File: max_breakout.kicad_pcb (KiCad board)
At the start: 4 copper layers, 51.1 x 25.7 mm, 47 parts, among them J1 USB_B_Micro, J2 Left, J3 AVR-JTAG-10, J4 Right, SW1 User, SW2 Reset, U1 LP2985-5.0, U2 LP2985-3.3, U4 MAX40203AUK+T, U5 74HCT125, U7 EPM7032STC44, U8 74HCT1G04, X1 CTX-636 50mhz

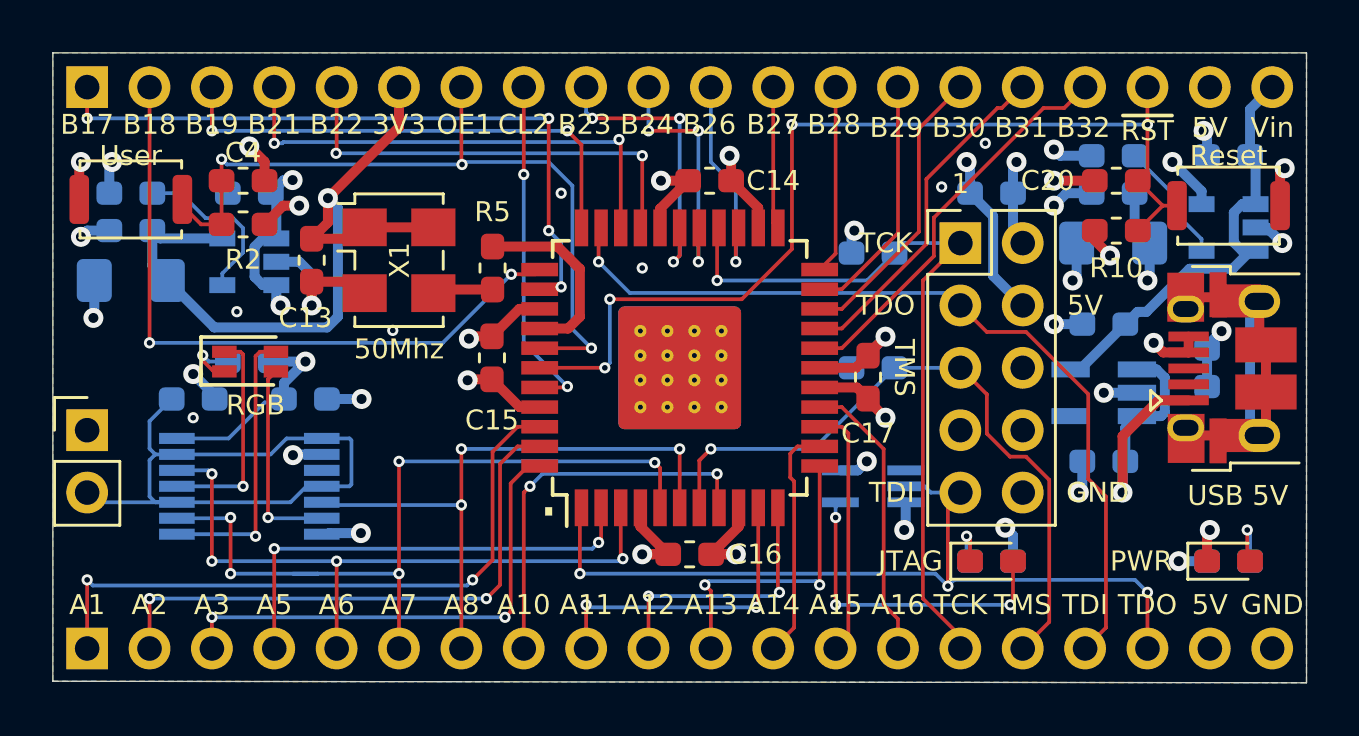
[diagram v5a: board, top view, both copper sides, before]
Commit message: removed extra cap from reg outputs
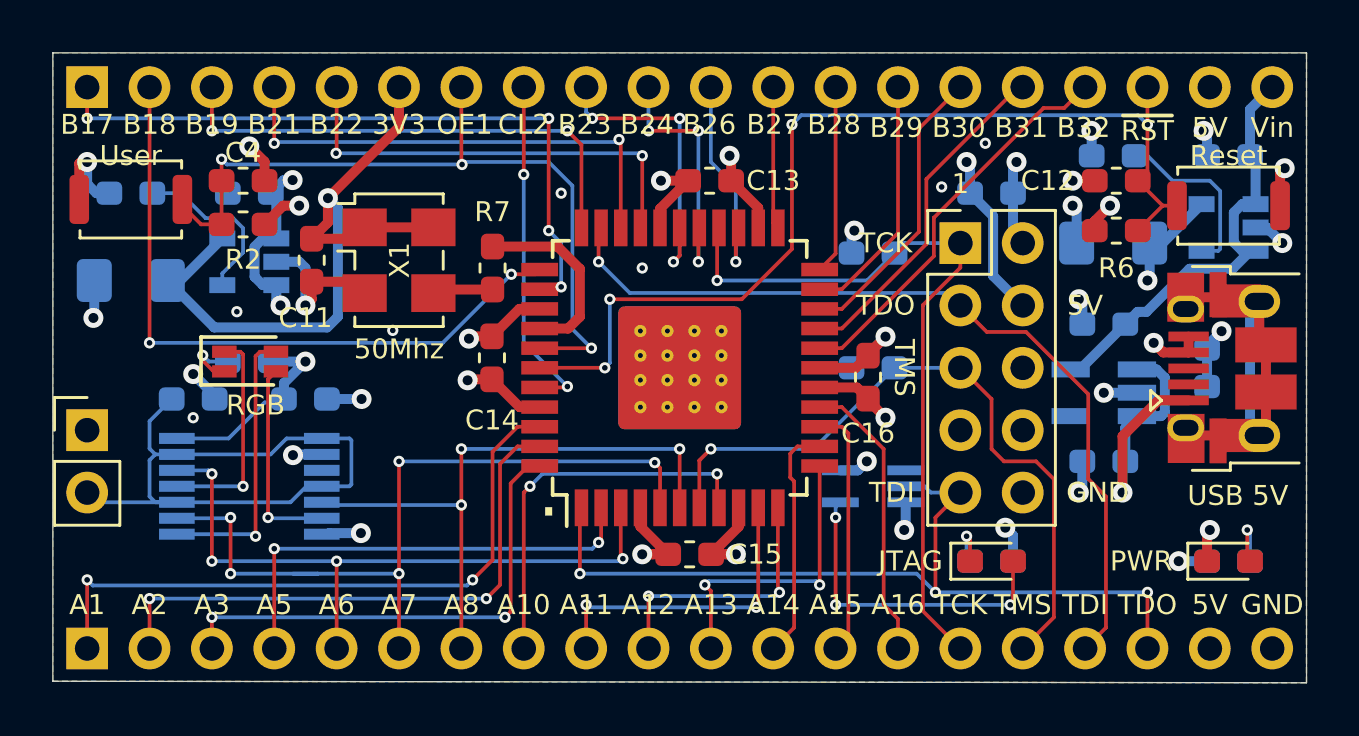
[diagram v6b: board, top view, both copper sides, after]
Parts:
- removed the C8 at (167.5, 97.0)
- removed the C9 at (127.5, 98.6)
- renumbered C12 to C10, C13 to C11, C20 to C12, C14 to C13, C15 to C14, C16 to C15, C17 to C16, C18 to C17, C19 to C18, C10 to C8, C11 to C9, R8 to R10, R9 to R3, R3 to R4, R4 to R5, R10 to R6, R5 to R7, R6 to R8, R7 to R9, U4 to U3, U5 to U4, U7 to U5, U8 to U6
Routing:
- net GND: track 58.9 -> 55.6 mm, vias 37 -> 34
- net 3V3: track 31.0 -> 28.7 mm
- net Net-(C6-Pad1): track 5.00 -> 7.23 mm
- net 5V: track 50.6 -> 49.0 mm, vias 15 -> 14
- net /TMS: track 27.9 -> 28.4 mm

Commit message: Replaced RGB with leds. Reorganized switches. pulldowns for OE and RST
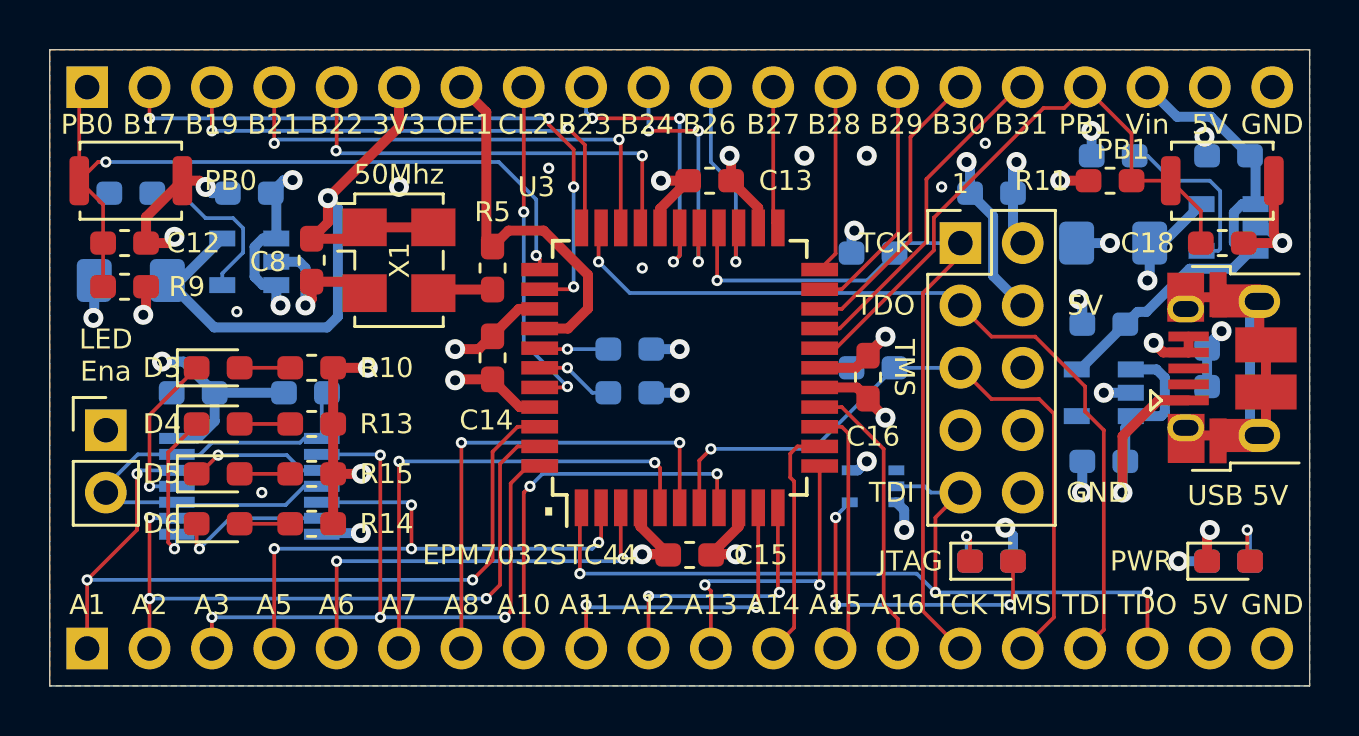
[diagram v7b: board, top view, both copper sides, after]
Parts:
- removed the C11 at (134.9, 99.8)
- removed the C4 at (132.1, 96.5)
- removed the J3 at (161.3, 99.1)
- removed the R2 at (132.1, 98.3)
- removed the U5 at (149.9, 104.1)
- added C18: 10nF, Capacitor_SMD:C_0603_1608Metric_Pad1.05x0.95mm_HandSolder, F.Cu at (172.0, 99.1)
- added C8: 100nF, Capacitor_SMD:C_0603_1608Metric_Pad1.05x0.95mm_HandSolder, F.Cu at (134.9, 99.8)
- added D4: Grn, LED_SMD:LED_0603_1608Metric_Pad1.05x0.95mm_HandSolder, F.Cu at (131.1, 106.4)
- added D5: Grn, LED_SMD:LED_0603_1608Metric_Pad1.05x0.95mm_HandSolder, F.Cu at (131.1, 108.5)
- added D6: Grn, LED_SMD:LED_0603_1608Metric_Pad1.05x0.95mm_HandSolder, F.Cu at (131.1, 110.5)
- added J2: AVR-JTAG-10, Connector_PinHeader_2.54mm:PinHeader_2x05_P2.54mm_Vertical, F.Cu at (161.3, 99.1)
- added R10: 360R, Resistor_SMD:R_0603_1608Metric_Pad1.05x0.95mm_HandSolder, F.Cu at (134.9, 104.1)
- added R11: 10K, Resistor_SMD:R_0603_1608Metric_Pad1.05x0.95mm_HandSolder, F.Cu at (167.4, 96.5)
- added R13: 360R, Resistor_SMD:R_0603_1608Metric_Pad1.05x0.95mm_HandSolder, F.Cu at (134.9, 106.4)
- added R14: 360R, Resistor_SMD:R_0603_1608Metric_Pad1.05x0.95mm_HandSolder, F.Cu at (134.9, 110.5)
- added R15: 360R, Resistor_SMD:R_0603_1608Metric_Pad1.05x0.95mm_HandSolder, F.Cu at (134.9, 108.5)
- added R9: 10K, Resistor_SMD:R_0603_1608Metric_Pad1.05x0.95mm_HandSolder, F.Cu at (127.3, 100.8)
- added U3: EPM7032STC44, Package_QFP:TQFP-44_10x10mm_P0.8mm, F.Cu at (149.9, 104.1)
- D1: value Red -> Green
- D2: value RGB -> Red; footprint LED_SMD:IN-S85TATRGB -> LED_SMD:LED_0603_1608Metric_Pad1.05x0.95mm_HandSolder
- D3: value Green -> Grn
- R5: value 360R -> 33R; moved to F.Cu
- R6: value 10K -> 1K; moved to B.Cu
- R7: value 33R -> 1K; moved to B.Cu
- SW2: value Reset -> User
- U1: renamed from U3; footprint Package_TO_SOT_SMD:SOT-23-5_HandSoldering -> Package_TO_SOT_SMD:SOT-23-5
- U2: renamed from U6; footprint Package_TO_SOT_SMD:SOT-353_SC-70-5_Handsoldering -> Package_TO_SOT_SMD:SOT-353_SC-70-5
- moved D2 40.7 mm to (172.2, 112.0)
- moved C12 40.5 mm to (127.3, 99.1), turned to 0 degrees
- moved D3 32.5 mm to (131.1, 104.1)
- moved R6 20.4 mm to (147.8, 103.4)
- moved R5 10.6 mm to (142.2, 100.1), turned to 90 degrees
- moved D1 9.65 mm to (162.6, 112.0)
- moved R7 7.55 mm to (147.8, 105.2), turned to 0 degrees
- moved C17 4.58 mm to (130.0, 105.2), turned to 180 degrees
- moved R12 4.58 mm to (134.6, 105.2), turned to 0 degrees
- moved SW2 1.05 mm to (172.0, 96.5)
- moved JP1 0.76 mm to (126.5, 106.7)
- moved SW1 0.76 mm to (127.5, 96.5), turned to 0 degrees
- renumbered C5 to C1, C7 to C10, C9 to C11, C10 to C2, C1 to C3, C2 to C4, C6 to C5, C8 to C6, C18 to C7, C3 to C9, J2 to J3, R10 to R1, R3 to R12, R1 to R2, R4 to R3, R8 to R4, R9 to R8, U1 to U4, U2 to U5, U4 to U6
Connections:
- C12 pad 1: /~RST -> /PB0
- D1 pad 1: GND -> Net-(D1-Pad1)
- D2 pad 1: Net-(D2-Pad1) -> GND
- J1 pad 2: (no net) -> Net-(J1-Pad2)
- J1 pad 3: (no net) -> Net-(J1-Pad3)
- J3 pad 4: /A5 -> /A4
- J4 pad 1: /B17 -> /PB0
- J4 pad 17: /B32 -> /PB1
- J4 pad 18: /~RST -> Vin
- J4 pad 2: /B18 -> /B17
- J4 pad 20: Vin -> GND
- J4 pad 7: /OE1 -> /CLK
- R1 pad 1: Net-(D3-Pad1) -> Net-(D1-Pad1)
- R3 pad 2: Net-(D1-Pad2) -> Net-(D2-Pad2)
- R5 pad 1: 5V -> Net-(R5-Pad1)
- R5 pad 2: Net-(D2-Pad3) -> /CLK
- R6 pad 1: 5V -> Net-(R6-Pad1)
- R6 pad 2: /~RST -> GND
- R7 pad 2: /CLK -> GND
- SW1 pad 1: /OE1 -> /PB0
- SW2 pad 1: /~RST -> /PB1
- U1 pad 4: (no net) -> Net-(U1-Pad4)
- U2 pad 4: Net-(D3-Pad2) -> Net-(D1-Pad2)
- U6 pad 11: Net-(D2-Pad1) -> Net-(D3-Pad1)
- U6 pad 12: /A6 -> /A1
- U6 pad 2: GND -> /A3
- U6 pad 3: (no net) -> Net-(D5-Pad1)
- U6 pad 5: /A8 -> /A4
- U6 pad 6: Net-(D2-Pad4) -> Net-(D6-Pad1)
- U6 pad 8: Net-(D2-Pad2) -> Net-(D4-Pad1)
- U6 pad 9: /A7 -> /A2
- X1 pad 3: Net-(R7-Pad1) -> Net-(R5-Pad1)
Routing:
- net /~RST: track 41.1 -> 0.00 mm, vias 4 -> 0
- net /OE1: track 31.6 -> 0.00 mm, vias 3 -> 0
- net /PB0: track 0.00 -> 31.1 mm, vias 0 -> 2
- net /B18: track 27.5 -> 0.00 mm, vias 2 -> 0
- net /PB1: track 0.00 -> 25.2 mm
- net /A4: track 0.00 -> 24.3 mm, vias 0 -> 4
- net /A5: track 18.8 -> 0.00 mm, vias 2 -> 0
- net /B32: track 16.1 -> 0.00 mm
- net /A7: track 32.4 -> 20.0 mm, vias 5 -> 2
- net Net-(D3-Pad2): track 13.2 -> 2.06 mm, vias 3 -> 0
- net Net-(D1-Pad2): track 2.63 -> 13.4 mm, vias 1 -> 3
- net /A6: track 27.2 -> 17.4 mm, vias 4 -> 2
- net /A3: track 20.2 -> 29.2 mm, vias 2 -> 4
- net Net-(D2-Pad1): track 8.87 -> 0.00 mm, vias 1 -> 0
- net Net-(D2-Pad2): track 11.5 -> 2.63 mm
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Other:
- board size 51.1 x 25.7 mm -> 51.3 x 25.9 mm
- board text added: "LED Ena"
- board text added: "PB0"
- board text added: "PB1"
- board text removed: "B18"
- board text removed: "B32"
- board text removed: "RGB"
- board text removed: "Reset"
- board text removed: "User"
- board text removed: "~RST"

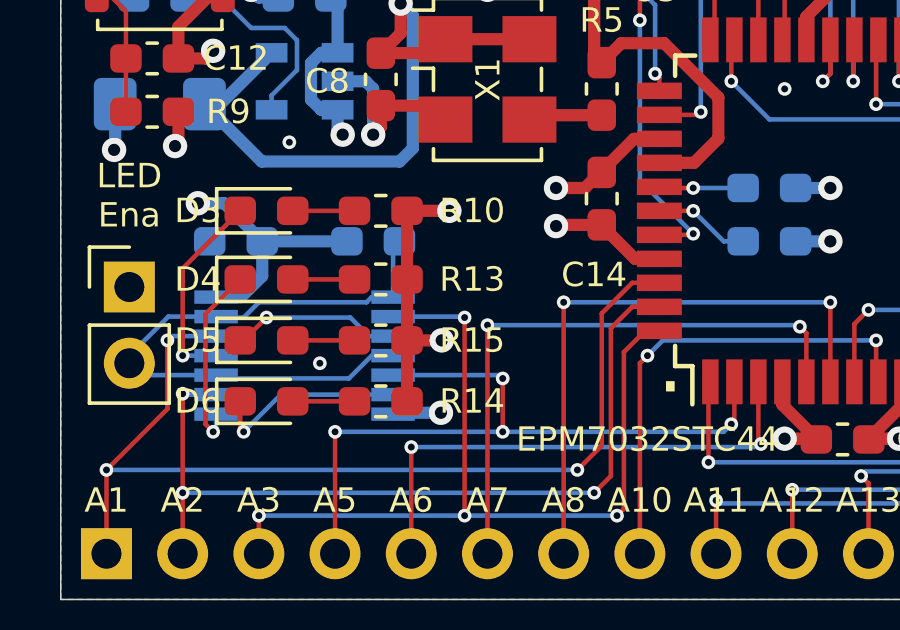
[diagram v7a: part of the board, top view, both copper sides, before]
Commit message: smaller footprint for IC2, fixed thermal vias
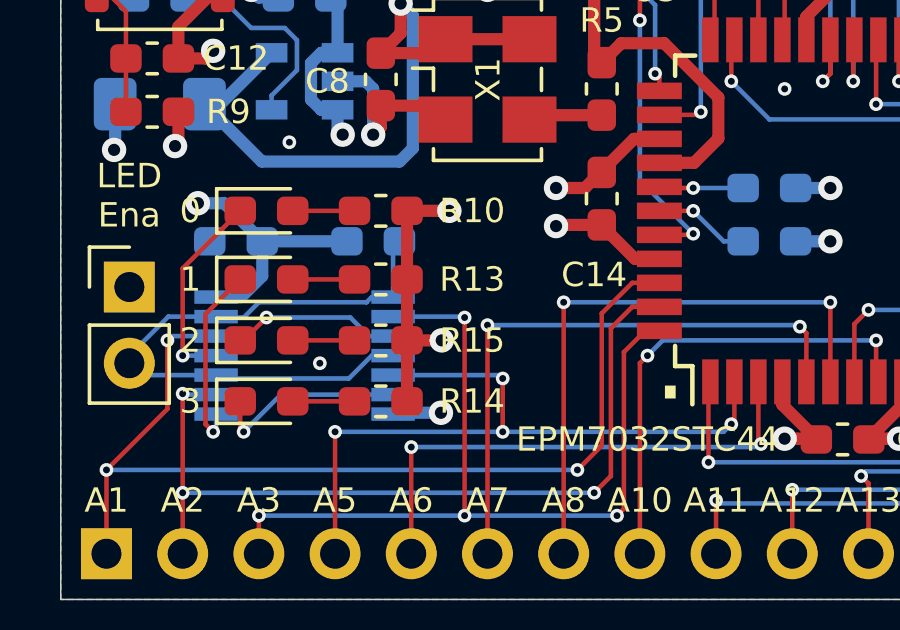
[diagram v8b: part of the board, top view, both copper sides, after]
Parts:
- renumbered D3 to 0, D4 to 1, D5 to 2, D6 to 3
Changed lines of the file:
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@@
   (layers
     (0 F.Cu signal)
-    (1 In1.Cu power hide)
-    (2 In2.Cu power hide)
+    (1 In1.Cu power)
+    (2 In2.Cu power)
     (31 B.Cu signal)
     (36 B.SilkS user)
-    (37 F.SilkS user hide)
-    (38 B.Mask user hide)
+    (37 F.SilkS user)
+    (38 B.Mask user)
     (39 F.Mask user)
     (44 Edge.Cuts user)
-    (45 Margin user hide)
+    (45 Margin user)
     (46 B.CrtYd user)
-    (47 F.CrtYd user hide)
+    (47 F.CrtYd user)
   )
   (setup
@@
     (tags "LED handsolder")
     (attr smd)
-    (fp_text reference D6 (at -2.286 0) (layer F.SilkS)
+    (fp_text reference 3 (at -2.54 0) (layer F.SilkS)
       (effects (font (size 0.8128 0.8128) (thickness 0.1524)))
     )
@@
     (tags "LED handsolder")
     (attr smd)
-    (fp_text reference D5 (at -2.286 0) (layer F.SilkS)
+    (fp_text reference 2 (at -2.54 0) (layer F.SilkS)
       (effects (font (size 0.8128 0.8128) (thickness 0.1524)))
     )
@@
     (tags "LED handsolder")
     (attr smd)
-    (fp_text reference D4 (at -2.286 0) (layer F.SilkS)
+    (fp_text reference 1 (at -2.54 0) (layer F.SilkS)
       (effects (font (size 0.8128 0.8128) (thickness 0.1524)))
     )
@@
     (tags "LED handsolder")
     (attr smd)
-    (fp_text reference D3 (at -2.286 0) (layer F.SilkS)
+    (fp_text reference 0 (at -2.54 0) (layer F.SilkS)
       (effects (font (size 0.8128 0.8128) (thickness 0.1524)))
     )
@@
   )
   (gr_text . (at 144.526 109.22) (layer F.SilkS)
-    (effects (font (size 2.032 2.032) (thickness 0.1524)))
+    (effects (font (size 2.54 2.54) (thickness 0.508)))
   )
   (gr_text B23 (at 145.987516 94.234) (layer F.SilkS)
